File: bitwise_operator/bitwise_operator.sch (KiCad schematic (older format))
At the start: 5 parts

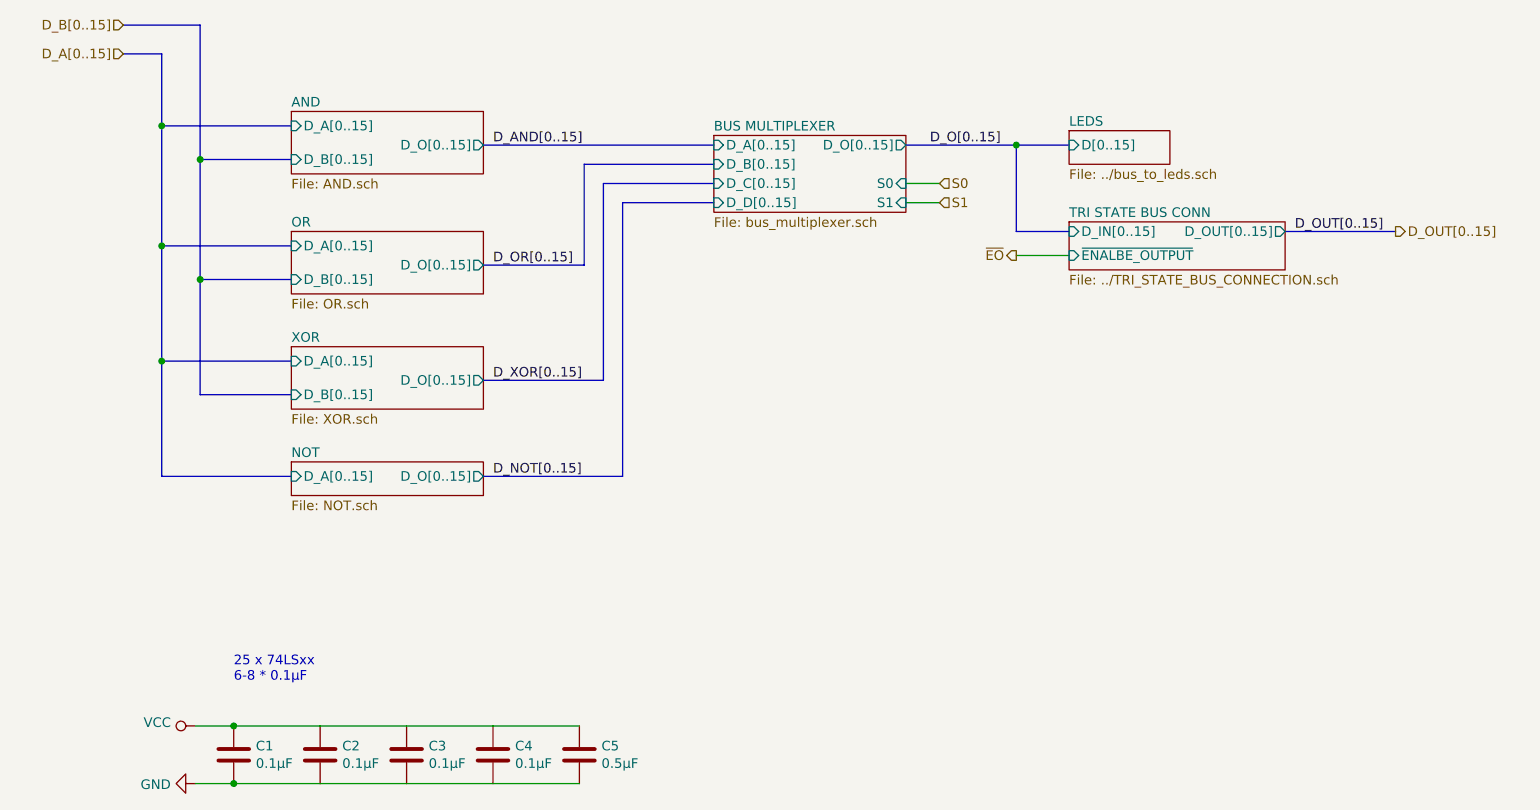
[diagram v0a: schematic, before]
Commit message: add bit operations
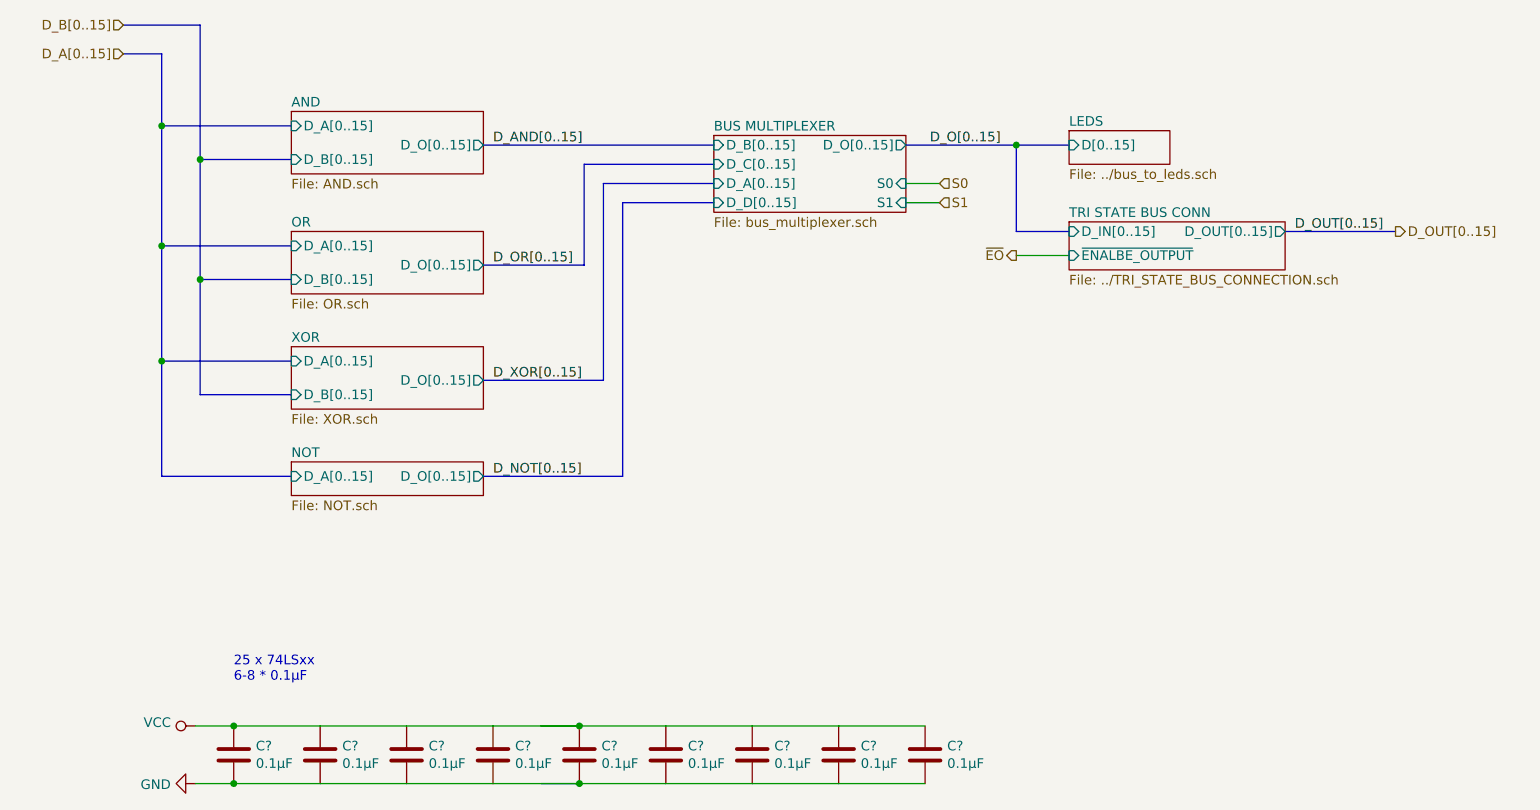
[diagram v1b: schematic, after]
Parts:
- removed C5: 0.5µF, Capacitor_THT:C_Disc_D4.3mm_W1.9mm_P5.00mm, symbol Device:C
- added C? (x5): 0.1µF, Capacitor_THT:C_Disc_D4.3mm_W1.9mm_P5.00mm, symbol Device:C
- renumbered C1 to C?, C2 to C?, C3 to C?, C4 to C?
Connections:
- wire segments 13 -> 23
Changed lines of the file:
@@
 EESchema Schematic File Version 4
+LIBS:computer-cache
 EELAYER 30 0
 EELAYER END
 $Descr A4 11693 8268
 encoding utf-8
-Sheet 2 13
+Sheet 2 29
 Title ""
 Date ""
@@
 Text Label 3775 3000 0    50   ~ 0
 D_XOR[0..15]
+Wire Bus Line
+	3725 1775 4925 1775
+Wire Bus Line
+	4250 2400 4250 1875
+Wire Bus Line
+	4250 1875 4925 1875
+Wire Bus Line
+	4350 3000 4350 1975
+Wire Bus Line
+	4350 1975 4925 1975
+Wire Bus Line
+	4925 2075 4450 2075
+Wire Bus Line
+	4450 2075 4450 3500
+Wire Bus Line
+	3725 3500 4450 3500
+Wire Wire Line
+	5925 1975 6100 1975
+Text HLabel 6100 1975 2    50   Input ~ 0
+S0
+Wire Wire Line
+	6100 2075 5925 2075
+Text HLabel 6100 2075 2    50   Input ~ 0
+S1
+$Sheet
+S 6775 1700 525  175
+U 5F633F15
+F0 "LEDS" 50
+F1 "../bus_to_leds.sch" 50
+F2 "D[0..15]" I L 6775 1775 50
+$EndSheet
+Wire Bus Line
+	6775 1775 6500 1775
+$Sheet
+S 6775 2175 1125 250
+U 5F6363FD
+F0 "TRI STATE BUS CONN" 50
+F1 "../TRI_STATE_BUS_CONNECTION.sch" 50
+F2 "~ENALBE_OUTPUT~" I L 6775 2350 50
+F3 "D_OUT[0..15]" O R 7900 2225 50
+F4 "D_IN[0..15]" I L 6775 2225 50
+$EndSheet
+Wire Bus Line
+	6500 1775 6500 2225
+Wire Bus Line
+	6500 2225 6775 2225
+Connection ~ 6500 1775
+Wire Bus Line
+	6500 1775 5925 1775
+Text Label 6050 1775 0    50   ~ 0
+D_O[0..15]
+Wire Bus Line
+	7900 2225 8475 2225
+Text HLabel 8475 2225 2    50   Output ~ 0
+D_OUT[0..15]
+Text Label 7950 2225 0    50   ~ 0
+D_OUT[0..15]
+$Comp
+L Device:C C?
+U 1 1 5F637C21
+P 2425 4950
+F 0 "C?" H 2540 4996 50  0000 L CNN
+F 1 "0.1µF" H 2540 4905 50  0000 L CNN
+F 2 "Capacitor_THT:C_Disc_D4.3mm_W1.9mm_P5.00mm" H 2463 4800 50  0001 C CNN
+F 3 "~" H 2425 4950 50  0001 C CNN
+	1    2425 4950
+	1    0    0    -1
+$EndComp
+$Comp
+L Device:C C?
+U 1 1 5F63A4EB
+P 2875 4950
+F 0 "C?" H 2990 4996 50  0000 L CNN
+F 1 "0.1µF" H 2990 4905 50  0000 L CNN
+F 2 "Capacitor_THT:C_Disc_D4.3mm_W1.9mm_P5.00mm" H 2913 4800 50  0001 C CNN
+F 3 "~" H 2875 4950 50  0001 C CNN
+	1    2875 4950
+	1    0    0    -1
+$EndComp
+Wire Wire Line
+	2875 5100 2425 5100
+Wire Wire Line
+	2425 4800 2875 4800
+Wire Wire Line
+	2425 4800 2225 4800
+Connection ~ 2425 4800
+$Comp
+L power:VCC #PWR?
+U 1 1 5F63B418
+P 2225 4800
+F 0 "#PWR?" H 2225 4650 50  0001 C CNN
+F 1 "VCC" V 2243 4927 50  0000 L CNN
+F 2 "" H 2225 4800 50  0001 C CNN
+F 3 "" H 2225 4800 50  0001 C CNN
+	1    2225 4800
+	0    -1   -1   0
+$EndComp
+Wire Wire Line
+	2425 5100 2225 5100
+Connection ~ 2425 5100
+$Comp
+L power:GND #PWR?
+U 1 1 5F63BA5A
+P 2225 5100
+F 0 "#PWR?" H 2225 4850 50  0001 C CNN
+F 1 "GND" V 2230 4972 50  0000 R CNN
+F 2 "" H 2225 5100 50  0001 C CNN
+F 3 "" H 2225 5100 50  0001 C CNN
+	1    2225 5100
+	0    1    1    0
+$EndComp
+Text Notes 2425 4575 0    50   ~ 0
+25 x 74LSxx\n6-8 * 0.1µF
+$Comp
+L Device:C C?
+U 1 1 5F63F8F0
+P 3325 4950
+F 0 "C?" H 3440 4996 50  0000 L CNN
+F 1 "0.1µF" H 3440 4905 50  0000 L CNN
+F 2 "Capacitor_THT:C_Disc_D4.3mm_W1.9mm_P5.00mm" H 3363 4800 50  0001 C CNN
+F 3 "~" H 3325 4950 50  0001 C CNN
+	1    3325 4950
+	1    0    0    -1
+$EndComp
+Wire Wire Line
+	3325 5100 2875 5100
+Wire Wire Line
+	2875 4800 3325 4800
+$Comp
+L Device:C C?
+U 1 1 5F6403F6
+P 3775 4950
+F 0 "C?" H 3890 4996 50  0000 L CNN
+F 1 "0.1µF" H 3890 4905 50  0000 L CNN
+F 2 "Capacitor_THT:C_Disc_D4.3mm_W1.9mm_P5.00mm" H 3813 4800 50  0001 C CNN
+F 3 "~" H 3775 4950 50  0001 C CNN
+	1    3775 4950
+	1    0    0    -1
+$EndComp
+Wire Wire Line
+	3775 5100 3325 5100
+Wire Wire Line
+	3325 4800 3775 4800
+Wire Wire Line
+	4225 5100 3775 5100
+Wire Wire Line
+	3775 4800 4225 4800
+Text HLabel 6500 2350 0    50   Output ~ 0
+~EO~
+Wire Wire Line
+	6500 2350 6775 2350
 $Sheet
 S 4925 1725 1000 400
@@
 F4 "S0" I R 5925 1975 50
 F5 "D_D[0..15]" I L 4925 2075 50
-F6 "D_C[0..15]" I L 4925 1975 50
-F7 "D_B[0..15]" I L 4925 1875 50
-F8 "D_A[0..15]" I L 4925 1775 50
-$EndSheet
-Wire Bus Line
-	3725 1775 4925 1775
-Wire Bus Line
-	4250 2400 4250 1875
-Wire Bus Line
-	4250 1875 4925 1875
-Wire Bus Line
-	4350 3000 4350 1975
-Wire Bus Line
-	4350 1975 4925 1975
-Wire Bus Line
-	4925 2075 4450 2075
-Wire Bus Line
-	4450 2075 4450 3500
-Wire Bus Line
-	3725 3500 4450 3500
-Wire Wire Line
-	5925 1975 6100 1975
-Text HLabel 6100 1975 2    50   Input ~ 0
-S0
-Wire Wire Line
-	6100 2075 5925 2075
-Text HLabel 6100 2075 2    50   Input ~ 0
-S1
-$Sheet
-S 6775 1700 525  175
-U 5F633F15
-F0 "LEDS" 50
-F1 "../bus_to_leds.sch" 50
-F2 "D[0..15]" I L 6775 1775 50
-$EndSheet
-Wire Bus Line
-	6775 1775 6500 1775
-$Sheet
-S 6775 2175 1125 250
-U 5F6363FD
-F0 "TRI STATE BUS CONN" 50
-F1 "../TRI_STATE_BUS_CONNECTION.sch" 50
-F2 "~ENALBE_OUTPUT~" I L 6775 2350 50
-F3 "D_OUT[0..15]" O R 7900 2225 50
-F4 "D_IN[0..15]" I L 6775 2225 50
-$EndSheet
-Wire Bus Line
-	6500 1775 6500 2225
-Wire Bus Line
-	6500 2225 6775 2225
-Connection ~ 6500 1775
-Wire Bus Line
-	6500 1775 5925 1775
-Text Label 6050 1775 0    50   ~ 0
-D_O[0..15]
-Wire Bus Line
-	7900 2225 8475 2225
-Text HLabel 8475 2225 2    50   Output ~ 0
-D_OUT[0..15]
-Text Label 7950 2225 0    50   ~ 0
-D_OUT[0..15]
-$Comp
-L Device:C C1
-U 1 1 5F637C21
-P 2425 4950
-F 0 "C1" H 2540 4996 50  0000 L CNN
-F 1 "0.1µF" H 2540 4905 50  0000 L CNN
-F 2 "Capacitor_THT:C_Disc_D4.3mm_W1.9mm_P5.00mm" H 2463 4800 50  0001 C CNN
-F 3 "~" H 2425 4950 50  0001 C CNN
-	1    2425 4950
-	1    0    0    -1
-$EndComp
-$Comp
-L Device:C C2
-U 1 1 5F63A4EB
-P 2875 4950
-F 0 "C2" H 2990 4996 50  0000 L CNN
-F 1 "0.1µF" H 2990 4905 50  0000 L CNN
-F 2 "Capacitor_THT:C_Disc_D4.3mm_W1.9mm_P5.00mm" H 2913 4800 50  0001 C CNN
-F 3 "~" H 2875 4950 50  0001 C CNN
-	1    2875 4950
-	1    0    0    -1
-$EndComp
-Wire Wire Line
-	2875 5100 2425 5100
-Wire Wire Line
-	2425 4800 2875 4800
-Wire Wire Line
-	2425 4800 2225 4800
-Connection ~ 2425 4800
-$Comp
-L power:VCC #PWR0101
-U 1 1 5F63B418
-P 2225 4800
-F 0 "#PWR0101" H 2225 4650 50  0001 C CNN
-F 1 "VCC" V 2243 4927 50  0000 L CNN
-F 2 "" H 2225 4800 50  0001 C CNN
-F 3 "" H 2225 4800 50  0001 C CNN
-	1    2225 4800
-	0    -1   -1   0
-$EndComp
-Wire Wire Line
-	2425 5100 2225 5100
-Connection ~ 2425 5100
-$Comp
-L power:GND #PWR0102
-U 1 1 5F63BA5A
-P 2225 5100
-F 0 "#PWR0102" H 2225 4850 50  0001 C CNN
-F 1 "GND" V 2230 4972 50  0000 R CNN
-F 2 "" H 2225 5100 50  0001 C CNN
-F 3 "" H 2225 5100 50  0001 C CNN
-	1    2225 5100
-	0    1    1    0
-$EndComp
-Text Notes 2425 4575 0    50   ~ 0
-25 x 74LSxx\n6-8 * 0.1µF
-$Comp
-L Device:C C3
-U 1 1 5F63F8F0
-P 3325 4950
-F 0 "C3" H 3440 4996 50  0000 L CNN
-F 1 "0.1µF" H 3440 4905 50  0000 L CNN
-F 2 "Capacitor_THT:C_Disc_D4.3mm_W1.9mm_P5.00mm" H 3363 4800 50  0001 C CNN
-F 3 "~" H 3325 4950 50  0001 C CNN
-	1    3325 4950
-	1    0    0    -1
-$EndComp
-Wire Wire Line
-	3325 5100 2875 5100
-Wire Wire Line
-	2875 4800 3325 4800
-$Comp
-L Device:C C4
-U 1 1 5F6403F6
-P 3775 4950
-F 0 "C4" H 3890 4996 50  0000 L CNN
-F 1 "0.1µF" H 3890 4905 50  0000 L CNN
-F 2 "Capacitor_THT:C_Disc_D4.3mm_W1.9mm_P5.00mm" H 3813 4800 50  0001 C CNN
-F 3 "~" H 3775 4950 50  0001 C CNN
-	1    3775 4950
-	1    0    0    -1
-$EndComp
-Wire Wire Line
-	3775 5100 3325 5100
-Wire Wire Line
-	3325 4800 3775 4800
-$Comp
-L Device:C C5
-U 1 1 5F640B48
+F6 "D_C[0..15]" I L 4925 1875 50
+F7 "D_B[0..15]" I L 4925 1775 50
+F8 "D_A[0..15]" I L 4925 1975 50
+$EndSheet
+$Comp
+L Device:C C?
+U 1 1 5F26F574
 P 4225 4950
-F 0 "C5" H 4340 4996 50  0000 L CNN
-F 1 "0.5µF" H 4340 4905 50  0000 L CNN
+F 0 "C?" H 4340 4996 50  0000 L CNN
+F 1 "0.1µF" H 4340 4905 50  0000 L CNN
 F 2 "Capacitor_THT:C_Disc_D4.3mm_W1.9mm_P5.00mm" H 4263 4800 50  0001 C CNN
 F 3 "~" H 4225 4950 50  0001 C CNN
@@
 	1    0    0    -1
 $EndComp
-Wire Wire Line
-	4225 5100 3775 5100
-Wire Wire Line
-	3775 4800 4225 4800
-Text HLabel 6500 2350 0    50   Output ~ 0
-~EO~
-Wire Wire Line
-	6500 2350 6775 2350
+$Comp
+L Device:C C?
+U 1 1 5F26F57A
+P 4675 4950
+F 0 "C?" H 4790 4996 50  0000 L CNN
+F 1 "0.1µF" H 4790 4905 50  0000 L CNN
+F 2 "Capacitor_THT:C_Disc_D4.3mm_W1.9mm_P5.00mm" H 4713 4800 50  0001 C CNN
+F 3 "~" H 4675 4950 50  0001 C CNN
+	1    4675 4950
+	1    0    0    -1
+$EndComp
+Wire Wire Line
+	4675 5100 4225 5100
+Wire Wire Line
+	4225 4800 4675 4800
+Wire Wire Line
+	4225 4800 4025 4800
+Connection ~ 4225 4800
+Wire Wire Line
+	4225 5100 4025 5100
+Connection ~ 4225 5100
+$Comp
+L Device:C C?
+U 1 1 5F26F586
+P 5125 4950
+F 0 "C?" H 5240 4996 50  0000 L CNN
+F 1 "0.1µF" H 5240 4905 50  0000 L CNN
+F 2 "Capacitor_THT:C_Disc_D4.3mm_W1.9mm_P5.00mm" H 5163 4800 50  0001 C CNN
+F 3 "~" H 5125 4950 50  0001 C CNN
+	1    5125 4950
+	1    0    0    -1
+$EndComp
+Wire Wire Line
+	5125 5100 4675 5100
+Wire Wire Line
+	4675 4800 5125 4800
+$Comp
+L Device:C C?
+U 1 1 5F26F58E
+P 5575 4950
+F 0 "C?" H 5690 4996 50  0000 L CNN
+F 1 "0.1µF" H 5690 4905 50  0000 L CNN
+F 2 "Capacitor_THT:C_Disc_D4.3mm_W1.9mm_P5.00mm" H 5613 4800 50  0001 C CNN
+F 3 "~" H 5575 4950 50  0001 C CNN
+	1    5575 4950
+	1    0    0    -1
+$EndComp
+Wire Wire Line
+	5575 5100 5125 5100
+Wire Wire Line
+	5125 4800 5575 4800
+Wire Wire Line
+	6025 5100 5575 5100
+Wire Wire Line
+	5575 4800 6025 4800
+$Comp
+L Device:C C?
+U 1 1 5F26FFBA
+P 6025 4950
+F 0 "C?" H 6140 4996 50  0000 L CNN
+F 1 "0.1µF" H 6140 4905 50  0000 L CNN
+F 2 "Capacitor_THT:C_Disc_D4.3mm_W1.9mm_P5.00mm" H 6063 4800 50  0001 C CNN
+F 3 "~" H 6025 4950 50  0001 C CNN
+	1    6025 4950
+	1    0    0    -1
+$EndComp
 $EndSCHEMATC

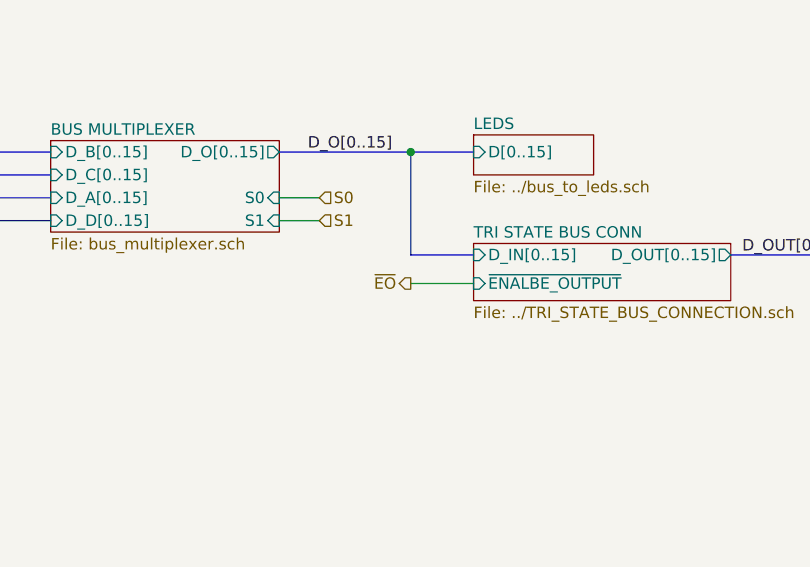
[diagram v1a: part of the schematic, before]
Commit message: memory programmer and cu
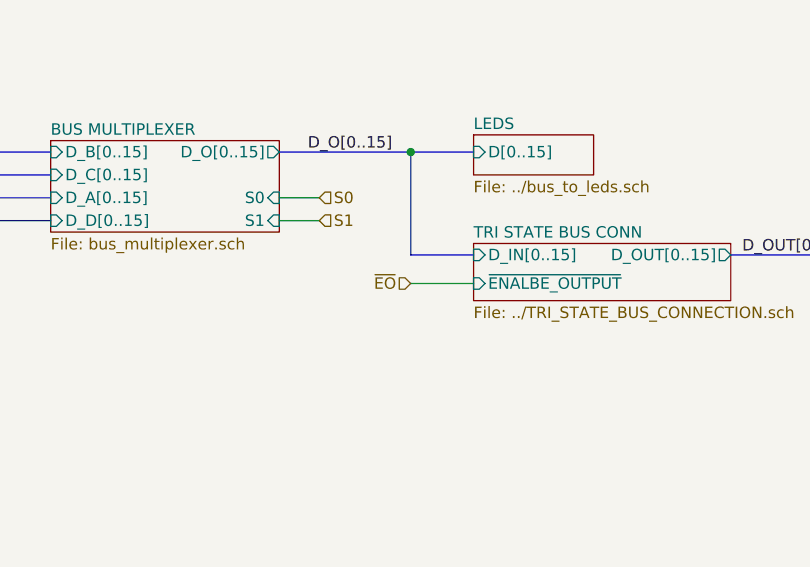
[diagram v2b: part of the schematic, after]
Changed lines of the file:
@@
 Wire Wire Line
 	3775 4800 4225 4800
-Text HLabel 6500 2350 0    50   Output ~ 0
+Text HLabel 6500 2350 0    50   Input ~ 0
 ~EO~
 Wire Wire Line

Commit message: part lists
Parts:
- added C10: 0.1µF, Capacitor_THT:C_Disc_D4.3mm_W1.9mm_P5.00mm, symbol Device:C
- gave numbers to parts that had none: 9
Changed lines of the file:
@@
 EESchema Schematic File Version 4
-LIBS:computer-cache
+LIBS:bitwise_operator_pcb-cache
 EELAYER 30 0
 EELAYER END
 $Descr A4 11693 8268
 encoding utf-8
-Sheet 2 36
+Sheet 2 13
 Title ""
 Date ""
@@
 D_OUT[0..15]
 $Comp
-L Device:C C?
+L Device:C C1
 U 1 1 5F637C21
 P 2425 4950
-F 0 "C?" H 2540 4996 50  0000 L CNN
+F 0 "C1" H 2540 4996 50  0000 L CNN
 F 1 "0.1µF" H 2540 4905 50  0000 L CNN
 F 2 "Capacitor_THT:C_Disc_D4.3mm_W1.9mm_P5.00mm" H 2463 4800 50  0001 C CNN
@@
 $EndComp
 $Comp
-L Device:C C?
+L Device:C C2
 U 1 1 5F63A4EB
 P 2875 4950
-F 0 "C?" H 2990 4996 50  0000 L CNN
+F 0 "C2" H 2990 4996 50  0000 L CNN
 F 1 "0.1µF" H 2990 4905 50  0000 L CNN
 F 2 "Capacitor_THT:C_Disc_D4.3mm_W1.9mm_P5.00mm" H 2913 4800 50  0001 C CNN
@@
 Connection ~ 2425 4800
 $Comp
-L power:VCC #PWR?
+L power:VCC #PWR01
 U 1 1 5F63B418
 P 2225 4800
-F 0 "#PWR?" H 2225 4650 50  0001 C CNN
+F 0 "#PWR01" H 2225 4650 50  0001 C CNN
 F 1 "VCC" V 2243 4927 50  0000 L CNN
 F 2 "" H 2225 4800 50  0001 C CNN
@@
 Connection ~ 2425 5100
 $Comp
-L power:GND #PWR?
+L power:GND #PWR02
 U 1 1 5F63BA5A
 P 2225 5100
-F 0 "#PWR?" H 2225 4850 50  0001 C CNN
+F 0 "#PWR02" H 2225 4850 50  0001 C CNN
 F 1 "GND" V 2230 4972 50  0000 R CNN
 F 2 "" H 2225 5100 50  0001 C CNN
@@
 25 x 74LSxx\n6-8 * 0.1µF
 $Comp
-L Device:C C?
+L Device:C C3
 U 1 1 5F63F8F0
 P 3325 4950
-F 0 "C?" H 3440 4996 50  0000 L CNN
+F 0 "C3" H 3440 4996 50  0000 L CNN
 F 1 "0.1µF" H 3440 4905 50  0000 L CNN
 F 2 "Capacitor_THT:C_Disc_D4.3mm_W1.9mm_P5.00mm" H 3363 4800 50  0001 C CNN
@@
 	2875 4800 3325 4800
 $Comp
-L Device:C C?
+L Device:C C4
 U 1 1 5F6403F6
 P 3775 4950
-F 0 "C?" H 3890 4996 50  0000 L CNN
+F 0 "C4" H 3890 4996 50  0000 L CNN
 F 1 "0.1µF" H 3890 4905 50  0000 L CNN
 F 2 "Capacitor_THT:C_Disc_D4.3mm_W1.9mm_P5.00mm" H 3813 4800 50  0001 C CNN
@@
 Wire Wire Line
 	3325 4800 3775 4800
-Wire Wire Line
-	4225 5100 3775 5100
-Wire Wire Line
-	3775 4800 4225 4800
 Text HLabel 6500 2350 0    50   Input ~ 0
 ~EO~
@@
 $EndSheet
 $Comp
-L Device:C C?
+L Device:C C5
 U 1 1 5F26F574
 P 4225 4950
-F 0 "C?" H 4340 4996 50  0000 L CNN
+F 0 "C5" H 4340 4996 50  0000 L CNN
 F 1 "0.1µF" H 4340 4905 50  0000 L CNN
 F 2 "Capacitor_THT:C_Disc_D4.3mm_W1.9mm_P5.00mm" H 4263 4800 50  0001 C CNN
@@
 $EndComp
 $Comp
-L Device:C C?
+L Device:C C6
 U 1 1 5F26F57A
 P 4675 4950
-F 0 "C?" H 4790 4996 50  0000 L CNN
+F 0 "C6" H 4790 4996 50  0000 L CNN
 F 1 "0.1µF" H 4790 4905 50  0000 L CNN
 F 2 "Capacitor_THT:C_Disc_D4.3mm_W1.9mm_P5.00mm" H 4713 4800 50  0001 C CNN
@@
 Wire Wire Line
 	4225 4800 4675 4800
-Wire Wire Line
-	4225 4800 4025 4800
 Connection ~ 4225 4800
-Wire Wire Line
-	4225 5100 4025 5100
-Connection ~ 4225 5100
-$Comp
-L Device:C C?
+$Comp
+L Device:C C7
 U 1 1 5F26F586
 P 5125 4950
-F 0 "C?" H 5240 4996 50  0000 L CNN
+F 0 "C7" H 5240 4996 50  0000 L CNN
 F 1 "0.1µF" H 5240 4905 50  0000 L CNN
 F 2 "Capacitor_THT:C_Disc_D4.3mm_W1.9mm_P5.00mm" H 5163 4800 50  0001 C CNN
@@
 	4675 4800 5125 4800
 $Comp
-L Device:C C?
+L Device:C C8
 U 1 1 5F26F58E
 P 5575 4950
-F 0 "C?" H 5690 4996 50  0000 L CNN
+F 0 "C8" H 5690 4996 50  0000 L CNN
 F 1 "0.1µF" H 5690 4905 50  0000 L CNN
 F 2 "Capacitor_THT:C_Disc_D4.3mm_W1.9mm_P5.00mm" H 5613 4800 50  0001 C CNN
@@
 	5575 4800 6025 4800
 $Comp
-L Device:C C?
+L Device:C C9
 U 1 1 5F26FFBA
 P 6025 4950
-F 0 "C?" H 6140 4996 50  0000 L CNN
+F 0 "C9" H 6140 4996 50  0000 L CNN
 F 1 "0.1µF" H 6140 4905 50  0000 L CNN
 F 2 "Capacitor_THT:C_Disc_D4.3mm_W1.9mm_P5.00mm" H 6063 4800 50  0001 C CNN
@@
 	1    0    0    -1
 $EndComp
+Wire Wire Line
+	3775 4800 4225 4800
+Connection ~ 3775 4800
+Wire Wire Line
+	3775 5100 4225 5100
+Connection ~ 3775 5100
+Connection ~ 4225 5100
+Connection ~ 4675 5100
+Connection ~ 4675 4800
+Connection ~ 5125 4800
+Connection ~ 5125 5100
+Connection ~ 5575 5100
+Connection ~ 5575 4800
+Connection ~ 3325 4800
+Connection ~ 3325 5100
+Connection ~ 2875 5100
+Connection ~ 2875 4800
+Wire Wire Line
+	6475 5100 6025 5100
+Wire Wire Line
+	6025 4800 6475 4800
+$Comp
+L Device:C C10
+U 1 1 5F48B5C2
+P 6475 4950
+F 0 "C10" H 6590 4996 50  0000 L CNN
+F 1 "0.1µF" H 6590 4905 50  0000 L CNN
+F 2 "Capacitor_THT:C_Disc_D4.3mm_W1.9mm_P5.00mm" H 6513 4800 50  0001 C CNN
+F 3 "~" H 6475 4950 50  0001 C CNN
+	1    6475 4950
+	1    0    0    -1
+$EndComp
+Connection ~ 6025 4800
+Connection ~ 6025 5100
 $EndSCHEMATC
